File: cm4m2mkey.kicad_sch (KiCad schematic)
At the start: 26 parts, among them J8 1-2199119-6

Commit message: respin
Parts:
- renumbered C62 to C64, C63 to C65, C64 to C66, C65 to C67, C66 to C68, C67 to C69, C68 to C70, C69 to C71, C70 to C72, C71 to C73, C72 to C74, R44 to R47, R45 to R48, R46 to R49, R47 to R50, R48 to R51, R49 to R52, R50 to R53, R51 to R54, R52 to R55, R53 to R56, R54 to R57, R55 to R58, R56 to R59, R57 to R60
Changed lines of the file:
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@@
   (symbol (lib_id "Device:R_Small") (at 81.28 118.11 90) (unit 1)
     (in_bom yes) (on_board yes)
-    (property "Reference" "R44" (id 0) (at 74.93 116.84 90)
+    (property "Reference" "R47" (id 0) (at 74.93 116.84 90)
       (effects (font (size 1 1)) (justify right))
     )
@@
   (symbol (lib_id "Device:R_Small") (at 99.06 77.47 90) (unit 1)
     (in_bom yes) (on_board yes)
-    (property "Reference" "R51" (id 0) (at 92.71 76.2 90)
+    (property "Reference" "R54" (id 0) (at 92.71 76.2 90)
       (effects (font (size 1 1)) (justify right))
     )
@@
   (symbol (lib_id "Device:C_Small") (at 147.32 54.61 90) (unit 1)
     (in_bom yes) (on_board yes)
-    (property "Reference" "C64" (id 0) (at 146.05 53.34 90)
+    (property "Reference" "C66" (id 0) (at 146.05 53.34 90)
       (effects (font (size 1 1)) (justify left))
     )
@@
   (symbol (lib_id "Device:R_Small") (at 99.06 82.55 90) (unit 1)
     (in_bom yes) (on_board yes)
-    (property "Reference" "R52" (id 0) (at 92.71 81.28 90)
+    (property "Reference" "R55" (id 0) (at 92.71 81.28 90)
       (effects (font (size 1 1)) (justify right))
     )
@@
   (symbol (lib_id "Device:C_Small") (at 147.32 167.64 90) (unit 1)
     (in_bom yes) (on_board yes)
-    (property "Reference" "C72" (id 0) (at 146.05 166.37 90)
+    (property "Reference" "C74" (id 0) (at 146.05 166.37 90)
       (effects (font (size 1 1)) (justify left))
     )
@@
   (symbol (lib_id "Device:R_Small") (at 99.06 74.93 90) (unit 1)
     (in_bom yes) (on_board yes)
-    (property "Reference" "R50" (id 0) (at 92.71 73.66 90)
+    (property "Reference" "R53" (id 0) (at 92.71 73.66 90)
       (effects (font (size 1 1)) (justify right))
     )
@@
   (symbol (lib_id "Device:R_Small") (at 99.06 59.69 90) (unit 1)
     (in_bom yes) (on_board yes)
-    (property "Reference" "R46" (id 0) (at 93.345 58.801 90)
+    (property "Reference" "R49" (id 0) (at 93.345 58.801 90)
       (effects (font (size 1 1)) (justify right))
     )
@@
   (symbol (lib_id "Device:R_Small") (at 99.06 67.31 90) (unit 1)
     (in_bom yes) (on_board yes)
-    (property "Reference" "R48" (id 0) (at 92.71 66.04 90)
+    (property "Reference" "R51" (id 0) (at 92.71 66.04 90)
       (effects (font (size 1 1)) (justify right))
     )
@@
   (symbol (lib_id "Device:C_Small") (at 147.32 152.4 90) (unit 1)
     (in_bom yes) (on_board yes)
-    (property "Reference" "C68" (id 0) (at 146.05 151.13 90)
+    (property "Reference" "C70" (id 0) (at 146.05 151.13 90)
       (effects (font (size 1 1)) (justify left))
     )
@@
   (symbol (lib_id "Device:C_Small") (at 147.32 144.78 90) (unit 1)
     (in_bom yes) (on_board yes)
-    (property "Reference" "C66" (id 0) (at 146.05 143.51 90)
+    (property "Reference" "C68" (id 0) (at 146.05 143.51 90)
       (effects (font (size 1 1)) (justify left))
     )
@@
   (symbol (lib_id "Device:C_Small") (at 147.32 140.97 90) (unit 1)
     (in_bom yes) (on_board yes)
-    (property "Reference" "C65" (id 0) (at 146.05 139.7 90)
+    (property "Reference" "C67" (id 0) (at 146.05 139.7 90)
       (effects (font (size 1 1)) (justify left))
     )
@@
   (symbol (lib_id "Device:R_Small") (at 99.06 97.79 90) (unit 1)
     (in_bom yes) (on_board yes)
-    (property "Reference" "R56" (id 0) (at 92.71 96.52 90)
+    (property "Reference" "R59" (id 0) (at 92.71 96.52 90)
       (effects (font (size 1 1)) (justify right))
     )
@@
   (symbol (lib_id "Device:C_Small") (at 147.32 148.59 90) (unit 1)
     (in_bom yes) (on_board yes)
-    (property "Reference" "C67" (id 0) (at 146.05 147.32 90)
+    (property "Reference" "C69" (id 0) (at 146.05 147.32 90)
       (effects (font (size 1 1)) (justify left))
     )
@@
   (symbol (lib_id "Device:C_Small") (at 147.32 46.99 90) (unit 1)
     (in_bom yes) (on_board yes)
-    (property "Reference" "C62" (id 0) (at 146.05 45.72 90)
+    (property "Reference" "C64" (id 0) (at 146.05 45.72 90)
       (effects (font (size 1 1)) (justify left))
     )
@@
   (symbol (lib_id "power:GND") (at 90.17 153.67 0) (unit 1)
     (in_bom yes) (on_board yes)
-    (property "Reference" "#PWR049" (id 0) (at 90.17 160.02 0)
+    (property "Reference" "#PWR050" (id 0) (at 90.17 160.02 0)
       (effects (font (size 1.27 1.27)) hide)
     )
@@
   (symbol (lib_id "power:GND") (at 154.94 170.18 0) (unit 1)
     (in_bom yes) (on_board yes)
-    (property "Reference" "#PWR051" (id 0) (at 154.94 176.53 0)
+    (property "Reference" "#PWR052" (id 0) (at 154.94 176.53 0)
       (effects (font (size 1.27 1.27)) hide)
     )
@@
   (symbol (lib_id "Device:R_Small") (at 99.06 69.85 90) (unit 1)
     (in_bom yes) (on_board yes)
-    (property "Reference" "R49" (id 0) (at 92.71 68.58 90)
+    (property "Reference" "R52" (id 0) (at 92.71 68.58 90)
       (effects (font (size 1 1)) (justify right))
     )
@@
   (symbol (lib_id "Device:C_Small") (at 147.32 163.83 90) (unit 1)
     (in_bom yes) (on_board yes)
-    (property "Reference" "C71" (id 0) (at 146.05 162.56 90)
+    (property "Reference" "C73" (id 0) (at 146.05 162.56 90)
       (effects (font (size 1 1)) (justify left))
     )
@@
   (symbol (lib_id "Device:C_Small") (at 147.32 156.21 90) (unit 1)
     (in_bom yes) (on_board yes)
-    (property "Reference" "C69" (id 0) (at 146.05 154.94 90)
+    (property "Reference" "C71" (id 0) (at 146.05 154.94 90)
       (effects (font (size 1 1)) (justify left))
     )
@@
   (symbol (lib_id "power:GND") (at 154.94 57.15 0) (unit 1)
     (in_bom yes) (on_board yes)
-    (property "Reference" "#PWR050" (id 0) (at 154.94 63.5 0)
+    (property "Reference" "#PWR051" (id 0) (at 154.94 63.5 0)
       (effects (font (size 1.27 1.27)) hide)
     )
@@
   (symbol (lib_id "Device:R_Small") (at 99.06 90.17 90) (unit 1)
     (in_bom yes) (on_board yes)
-    (property "Reference" "R54" (id 0) (at 92.71 88.9 90)
+    (property "Reference" "R57" (id 0) (at 92.71 88.9 90)
       (effects (font (size 1 1)) (justify right))
     )
@@
   (symbol (lib_id "Device:R_Small") (at 99.06 62.23 90) (unit 1)
     (in_bom yes) (on_board yes)
-    (property "Reference" "R47" (id 0) (at 92.71 60.96 90)
+    (property "Reference" "R50" (id 0) (at 92.71 60.96 90)
       (effects (font (size 1 1)) (justify right))
     )
@@
   (symbol (lib_id "Device:C_Small") (at 147.32 50.8 90) (unit 1)
     (in_bom yes) (on_board yes)
-    (property "Reference" "C63" (id 0) (at 146.05 49.53 90)
+    (property "Reference" "C65" (id 0) (at 146.05 49.53 90)
       (effects (font (size 1 1)) (justify left))
     )
@@
   (symbol (lib_id "Device:R_Small") (at 81.28 125.73 90) (unit 1)
     (in_bom yes) (on_board yes)
-    (property "Reference" "R45" (id 0) (at 74.93 127 90)
+    (property "Reference" "R48" (id 0) (at 74.93 127 90)
       (effects (font (size 1 1)) (justify right))
     )
@@
   (symbol (lib_id "Device:R_Small") (at 99.06 100.33 90) (unit 1)
     (in_bom yes) (on_board yes)
-    (property "Reference" "R57" (id 0) (at 92.71 99.06 90)
+    (property "Reference" "R60" (id 0) (at 92.71 99.06 90)
       (effects (font (size 1 1)) (justify right))
     )
@@
   (symbol (lib_id "Device:C_Small") (at 147.32 160.02 90) (unit 1)
     (in_bom yes) (on_board yes)
-    (property "Reference" "C70" (id 0) (at 146.05 158.75 90)
+    (property "Reference" "C72" (id 0) (at 146.05 158.75 90)
       (effects (font (size 1 1)) (justify left))
     )
@@
   (symbol (lib_id "Device:R_Small") (at 99.06 85.09 90) (unit 1)
     (in_bom yes) (on_board yes)
-    (property "Reference" "R53" (id 0) (at 92.71 83.82 90)
+    (property "Reference" "R56" (id 0) (at 92.71 83.82 90)
       (effects (font (size 1 1)) (justify right))
     )
@@
   (symbol (lib_id "Device:R_Small") (at 99.06 92.71 90) (unit 1)
     (in_bom yes) (on_board yes)
-    (property "Reference" "R55" (id 0) (at 92.71 91.44 90)
-      (effects (font (size 1 1)) (justify right))
-    )
+    (property "Reference" "R58" (id 0) (at 92.71 91.44 90)
+      (effects (font (size 1 1)) (justify right))
+    )

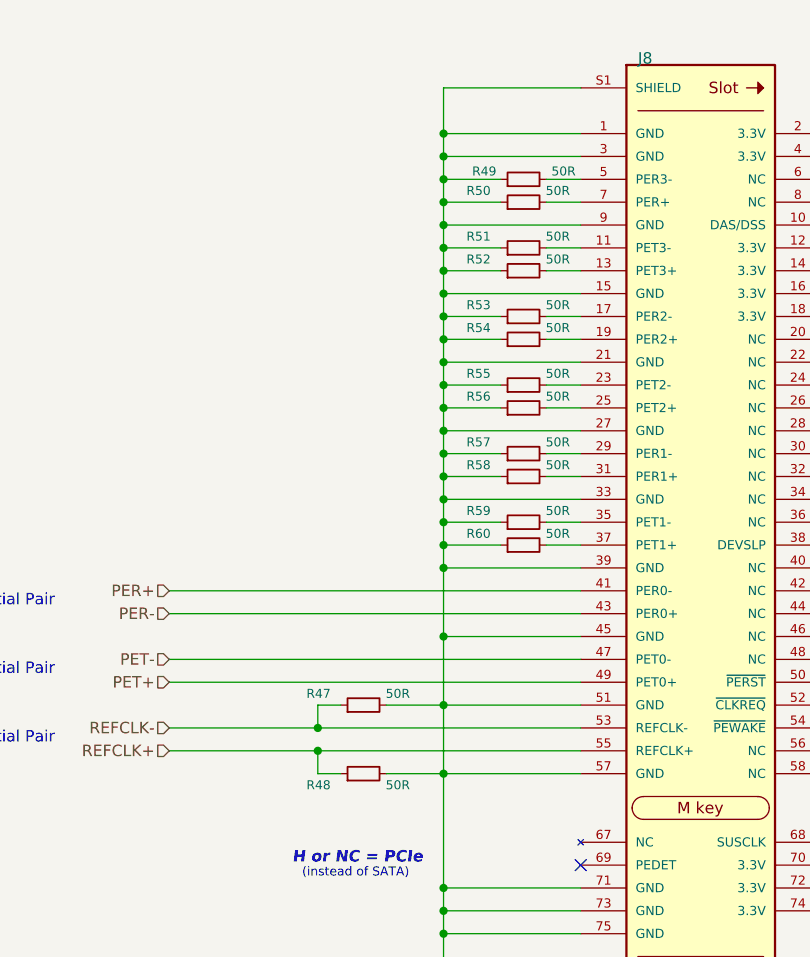
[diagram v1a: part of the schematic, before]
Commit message: fixed I2C ping indicator
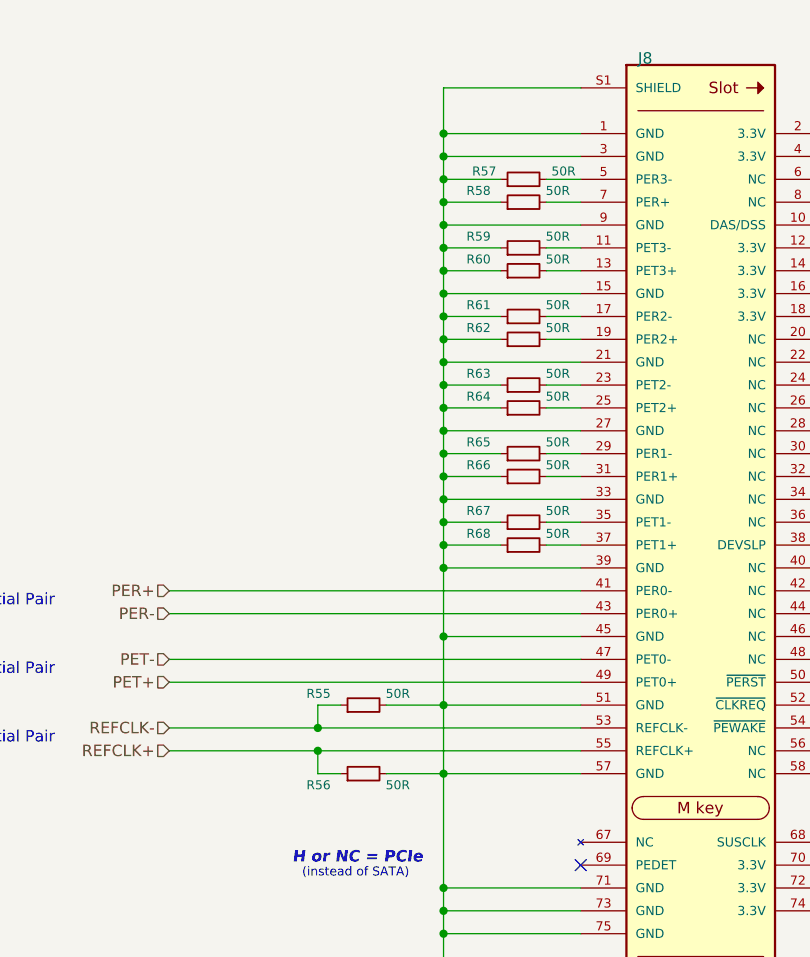
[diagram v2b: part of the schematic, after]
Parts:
- renumbered R47 to R55, R48 to R56, R49 to R57, R50 to R58, R51 to R59, R52 to R60, R53 to R61, R54 to R62, R55 to R63, R56 to R64, R57 to R65, R58 to R66, R59 to R67, R60 to R68
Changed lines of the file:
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@@
   (symbol (lib_id "Device:R_Small") (at 81.28 118.11 90) (unit 1)
     (in_bom yes) (on_board yes)
-    (property "Reference" "R47" (id 0) (at 74.93 116.84 90)
+    (property "Reference" "R55" (id 0) (at 74.93 116.84 90)
       (effects (font (size 1 1)) (justify right))
     )
@@
   (symbol (lib_id "Device:R_Small") (at 99.06 77.47 90) (unit 1)
     (in_bom yes) (on_board yes)
-    (property "Reference" "R54" (id 0) (at 92.71 76.2 90)
+    (property "Reference" "R62" (id 0) (at 92.71 76.2 90)
       (effects (font (size 1 1)) (justify right))
     )
@@
   (symbol (lib_id "Device:R_Small") (at 99.06 82.55 90) (unit 1)
     (in_bom yes) (on_board yes)
-    (property "Reference" "R55" (id 0) (at 92.71 81.28 90)
+    (property "Reference" "R63" (id 0) (at 92.71 81.28 90)
       (effects (font (size 1 1)) (justify right))
     )
@@
   (symbol (lib_id "Device:R_Small") (at 99.06 74.93 90) (unit 1)
     (in_bom yes) (on_board yes)
-    (property "Reference" "R53" (id 0) (at 92.71 73.66 90)
+    (property "Reference" "R61" (id 0) (at 92.71 73.66 90)
       (effects (font (size 1 1)) (justify right))
     )
@@
   (symbol (lib_id "Device:R_Small") (at 99.06 59.69 90) (unit 1)
     (in_bom yes) (on_board yes)
-    (property "Reference" "R49" (id 0) (at 93.345 58.801 90)
+    (property "Reference" "R57" (id 0) (at 93.345 58.801 90)
       (effects (font (size 1 1)) (justify right))
     )
@@
   (symbol (lib_id "Device:R_Small") (at 99.06 67.31 90) (unit 1)
     (in_bom yes) (on_board yes)
-    (property "Reference" "R51" (id 0) (at 92.71 66.04 90)
+    (property "Reference" "R59" (id 0) (at 92.71 66.04 90)
       (effects (font (size 1 1)) (justify right))
     )
@@
   (symbol (lib_id "Device:R_Small") (at 99.06 97.79 90) (unit 1)
     (in_bom yes) (on_board yes)
-    (property "Reference" "R59" (id 0) (at 92.71 96.52 90)
+    (property "Reference" "R67" (id 0) (at 92.71 96.52 90)
       (effects (font (size 1 1)) (justify right))
     )
@@
   (symbol (lib_id "power:GND") (at 90.17 153.67 0) (unit 1)
     (in_bom yes) (on_board yes)
-    (property "Reference" "#PWR050" (id 0) (at 90.17 160.02 0)
+    (property "Reference" "#PWR052" (id 0) (at 90.17 160.02 0)
       (effects (font (size 1.27 1.27)) hide)
     )
@@
   (symbol (lib_id "power:GND") (at 154.94 170.18 0) (unit 1)
     (in_bom yes) (on_board yes)
-    (property "Reference" "#PWR052" (id 0) (at 154.94 176.53 0)
+    (property "Reference" "#PWR054" (id 0) (at 154.94 176.53 0)
       (effects (font (size 1.27 1.27)) hide)
     )
@@
   (symbol (lib_id "Device:R_Small") (at 99.06 69.85 90) (unit 1)
     (in_bom yes) (on_board yes)
-    (property "Reference" "R52" (id 0) (at 92.71 68.58 90)
+    (property "Reference" "R60" (id 0) (at 92.71 68.58 90)
       (effects (font (size 1 1)) (justify right))
     )
@@
   (symbol (lib_id "power:GND") (at 154.94 57.15 0) (unit 1)
     (in_bom yes) (on_board yes)
-    (property "Reference" "#PWR051" (id 0) (at 154.94 63.5 0)
+    (property "Reference" "#PWR053" (id 0) (at 154.94 63.5 0)
       (effects (font (size 1.27 1.27)) hide)
     )
@@
   (symbol (lib_id "Device:R_Small") (at 99.06 90.17 90) (unit 1)
     (in_bom yes) (on_board yes)
-    (property "Reference" "R57" (id 0) (at 92.71 88.9 90)
+    (property "Reference" "R65" (id 0) (at 92.71 88.9 90)
       (effects (font (size 1 1)) (justify right))
     )
@@
   (symbol (lib_id "Device:R_Small") (at 99.06 62.23 90) (unit 1)
     (in_bom yes) (on_board yes)
-    (property "Reference" "R50" (id 0) (at 92.71 60.96 90)
+    (property "Reference" "R58" (id 0) (at 92.71 60.96 90)
       (effects (font (size 1 1)) (justify right))
     )
@@
   (symbol (lib_id "Device:R_Small") (at 81.28 125.73 90) (unit 1)
     (in_bom yes) (on_board yes)
-    (property "Reference" "R48" (id 0) (at 74.93 127 90)
+    (property "Reference" "R56" (id 0) (at 74.93 127 90)
       (effects (font (size 1 1)) (justify right))
     )
@@
   (symbol (lib_id "Device:R_Small") (at 99.06 100.33 90) (unit 1)
     (in_bom yes) (on_board yes)
-    (property "Reference" "R60" (id 0) (at 92.71 99.06 90)
+    (property "Reference" "R68" (id 0) (at 92.71 99.06 90)
       (effects (font (size 1 1)) (justify right))
     )
@@
   (symbol (lib_id "Device:R_Small") (at 99.06 85.09 90) (unit 1)
     (in_bom yes) (on_board yes)
-    (property "Reference" "R56" (id 0) (at 92.71 83.82 90)
+    (property "Reference" "R64" (id 0) (at 92.71 83.82 90)
       (effects (font (size 1 1)) (justify right))
     )
@@
   (symbol (lib_id "Device:R_Small") (at 99.06 92.71 90) (unit 1)
     (in_bom yes) (on_board yes)
-    (property "Reference" "R58" (id 0) (at 92.71 91.44 90)
-      (effects (font (size 1 1)) (justify right))
-    )
+    (property "Reference" "R66" (id 0) (at 92.71 91.44 90)
+      (effects (font (size 1 1)) (justify right))
+    )
